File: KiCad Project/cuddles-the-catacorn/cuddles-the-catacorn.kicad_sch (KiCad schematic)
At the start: 43 parts, among them J1 SAO, SW1 Left, SW2 Up, SW3 Right, SW4 Down, SW5 B, SW6 A, U1 SC0915

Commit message: First draft
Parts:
- removed D11, D12, D14, D15, D16: LED, LED_SMD:LED_0805_2012Metric_Pad1.15x1.40mm_HandSolder, symbol Device:LED
- removed R10, R6, R7, R8, R9: R470, Resistor_SMD:R_0805_2012Metric_Pad1.20x1.40mm_HandSolder, symbol Device:R
- removed SW3: Right, Button_Switch_SMD:SW_SPST_TL3342, symbol Switch:SW_Push
- removed SW4: Down, Button_Switch_SMD:SW_SPST_TL3342, symbol Switch:SW_Push
- added C6, C7, C8: C 0.1uF, Capacitor_SMD:C_0805_2012Metric_Pad1.18x1.45mm_HandSolder, symbol Device:C
- added D11, D12, D17: WS2812B, LED_SMD:LED_WS2812B_PLCC4_5.0x5.0mm_P3.2mm, symbol LED:WS2812B
- added J2, J3: Conn_01x05, Connector_PinHeader_2.54mm:PinHeader_1x05_P2.54mm_Vertical, symbol Connector_Generic:Conn_01x05
- H1, H2: footprint MountingHole:MountingHole_2.2mm_M2 -> MountingHole:MountingHole_2.2mm_M2_Pad
- SW1: value Left -> C
- SW2: value Up -> D
- renumbered SW5 to SW3, SW6 to SW4
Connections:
- net +3V3: now also C6.1, C7.1, C8.1, D11.1 (VDD), D12.1 (VDD), D17.1 (VDD)
- net GND: now also C6.2, C7.2, C8.2, D11.3 (VSS), D12.3 (VSS), D17.3 (VSS), J2.1 (Pin_1), J3.1 (Pin_1)
- net at SW3.1: now also U1.25 (I2C1_SCL/SPI0_TX/GP19); no longer U1.22 (UART0_RX/I2C0_SCL/SPI0_CSn/GP17)
- net at U1.20 (I2C1_SCL/SPI1_TX/GP15): now also R2.2, R3.2, R4.2
- net at D13.2 (A): now also R5.1
- net at D6.2 (DOUT): now also D17.4 (DIN)
- net at U1.24 (I2C1_SDA/SPI0_SCK/GP18): now also SW4.1
- net at U1.21 (UART0_TX/I2C0_SDA/SPI0_RX/GP16): no longer SW4.1
- net at U1.10 (I2C1_SCL/SPI0_TX/GP7): now also J2.2 (Pin_2)
- net at U1.11 (UART1_TX/I2C0_SDA/SPI1_RX/GP8): now also J3.5 (Pin_5)
- net at U1.12 (UART1_RX/I2C0_SCL/SPI1_CSn/GP9): now also J3.4 (Pin_4)
- net at U1.14 (I2C1_SDA/SPI1_SCK/GP10): now also J3.3 (Pin_3)
- net at U1.15 (I2C1_SCL/SPI1_TX/GP11): now also J3.2 (Pin_2)
- net at U1.17 (UART0_RX/I2C0_SCL/SPI1_CSn/GP13): now also R5.2
- net at U1.4 (I2C1_SDA/SPI0_SCK/GP2): now also J2.5 (Pin_5)
- net at U1.5 (I2C1_SCL/SPI0_TX/GP3): now also J2.4 (Pin_4)
- net at U1.9 (I2C1_SDA/SPI0_SCK/GP6): now also J2.3 (Pin_3)
- new net: R1.2, U1.19 (I2C1_SDA/SPI1_SCK/GP14)
- new net: D11.2 (DOUT), D12.4 (DIN)
- new net: D11.4 (DIN), D17.2 (DOUT)
- no-connect marks 19 -> 12
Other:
- note added: "Controls"
- note added: "Horn LED"
- note added: "Nose LED"
- note added: "Tail LEDs"
- note removed: "Gamepad Controls"
- note removed: "Left LEDs"
- note removed: "Right LEDs"
- title: Molly the Mermaid -> Cuddles the Catacorn
- moved on the sheet: J1, SW3, SW4

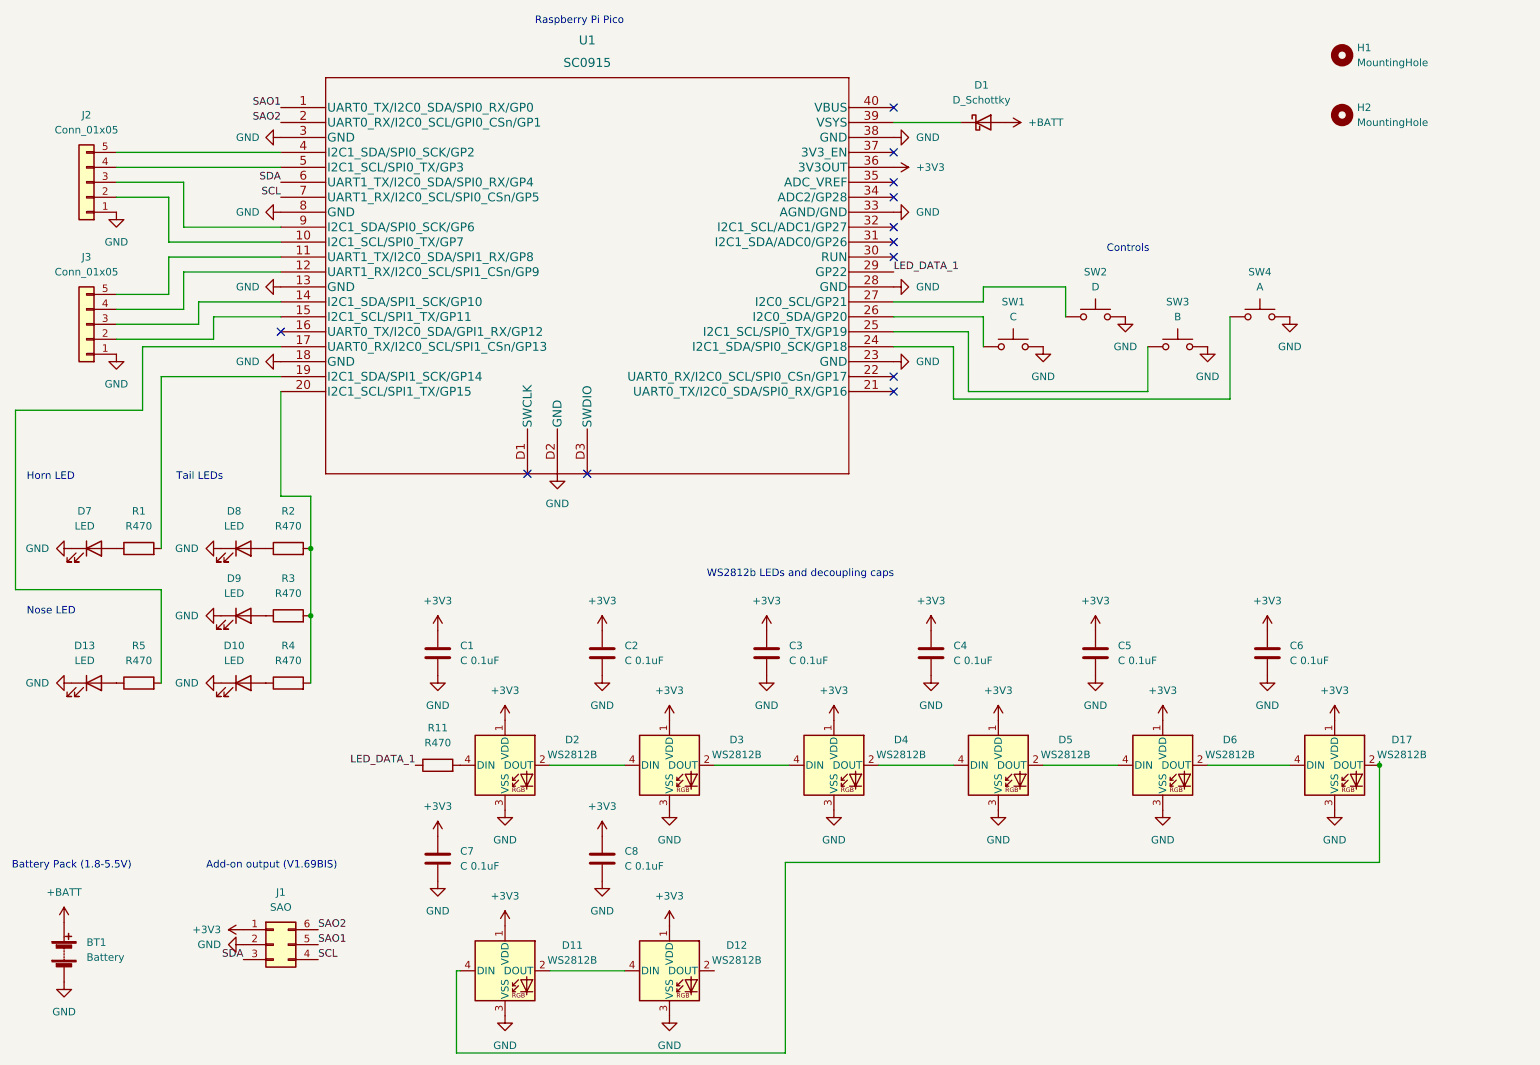
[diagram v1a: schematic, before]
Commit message: Schematic changes to simplify routing
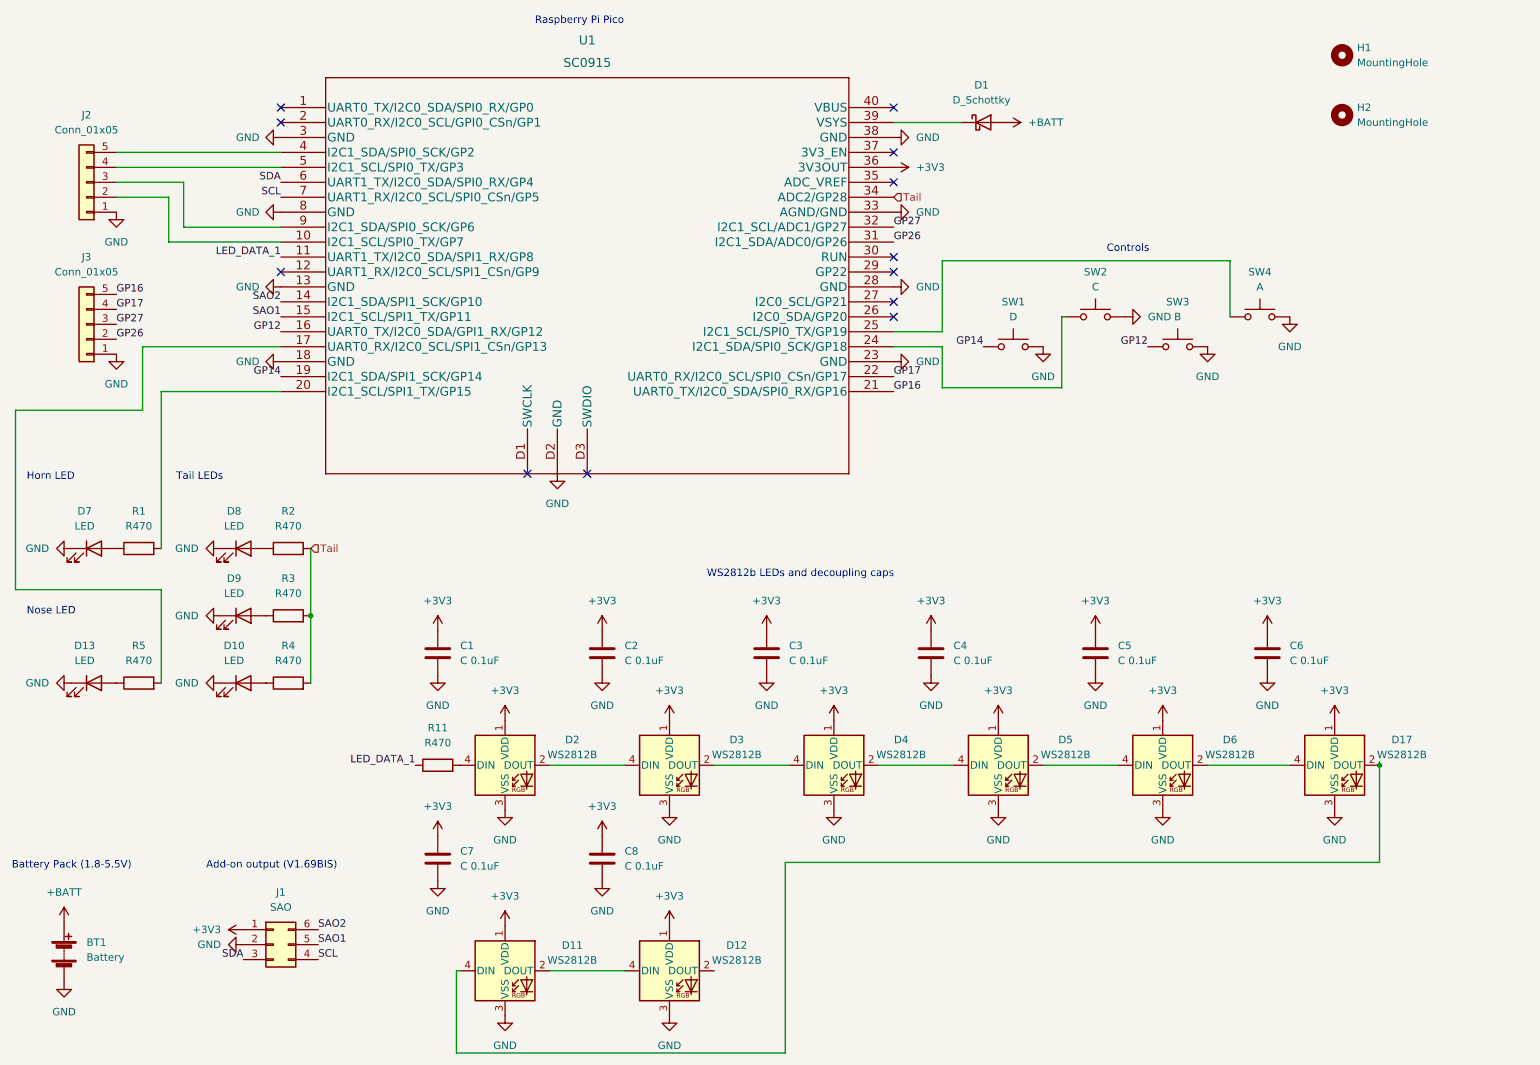
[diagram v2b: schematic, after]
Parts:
- SW1: value C -> D
- SW2: value D -> C
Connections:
- net LED_DATA_1: now also U1.11 (UART1_TX/I2C0_SDA/SPI1_RX/GP8); no longer U1.29 (GP22)
- net SAO1: now also U1.15 (I2C1_SCL/SPI1_TX/GP11); no longer U1.1 (UART0_TX/I2C0_SDA/SPI0_RX/GP0)
- net SAO2: now also U1.14 (I2C1_SDA/SPI1_SCK/GP10); no longer U1.2 (UART0_RX/I2C0_SCL/GPI0_CSn/GP1)
- net at U1.25 (I2C1_SCL/SPI0_TX/GP19): now also SW4.1; no longer SW3.1
- net Tail: now reaches R2.2, R3.2, R4.2
- net Tail: now also U1.34 (ADC2/GP28); no longer U1.20 (I2C1_SCL/SPI1_TX/GP15)
- net at U1.26 (I2C0_SDA/GP20): no longer SW1.1
- net at R1.2: now also U1.20 (I2C1_SCL/SPI1_TX/GP15); no longer U1.19 (I2C1_SDA/SPI1_SCK/GP14)
- net at U1.24 (I2C1_SDA/SPI0_SCK/GP18): now also SW2.1; no longer SW4.1
- net GP16: now reaches J3.5 (Pin_5)
- net GP16: now also U1.21 (UART0_TX/I2C0_SDA/SPI0_RX/GP16); no longer U1.11 (UART1_TX/I2C0_SDA/SPI1_RX/GP8)
- net at U1.12 (UART1_RX/I2C0_SCL/SPI1_CSn/GP9): no longer J3.4 (Pin_4)
- net GP27: now reaches J3.3 (Pin_3)
- net GP27: now also U1.32 (I2C1_SCL/ADC1/GP27); no longer U1.14 (I2C1_SDA/SPI1_SCK/GP10)
- net GP26: now reaches J3.2 (Pin_2)
- net GP26: now also U1.31 (I2C1_SDA/ADC0/GP26); no longer U1.15 (I2C1_SCL/SPI1_TX/GP11)
- net GP12: now reaches U1.16 (UART0_TX/I2C0_SDA/GPI1_RX/GP12)
- net GP12: now also SW3.1
- net GP17: now reaches U1.22 (UART0_RX/I2C0_SCL/SPI0_CSn/GP17)
- net GP17: now also J3.4 (Pin_4)
- net at U1.27 (I2C0_SCL/GP21): no longer SW2.1
- new net GP14: SW1.1, U1.19 (I2C1_SDA/SPI1_SCK/GP14)
